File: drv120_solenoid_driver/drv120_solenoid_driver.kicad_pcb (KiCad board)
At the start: 2 copper layers, 23.6 x 13 mm, 9 parts, among them J1 +PWR-, J2 +EN-, J3 SOLENOID, U1 drv120

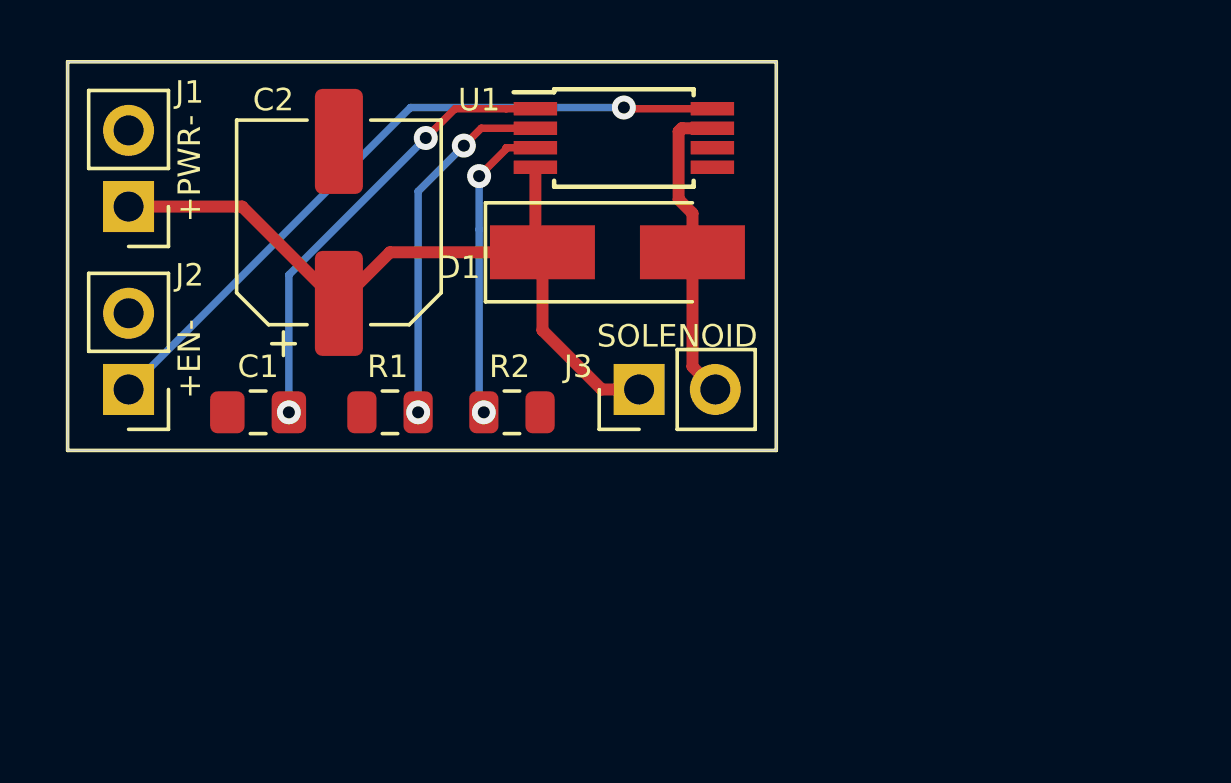
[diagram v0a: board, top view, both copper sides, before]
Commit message: Tab mounting version
PCB design with mounting tabs on either side
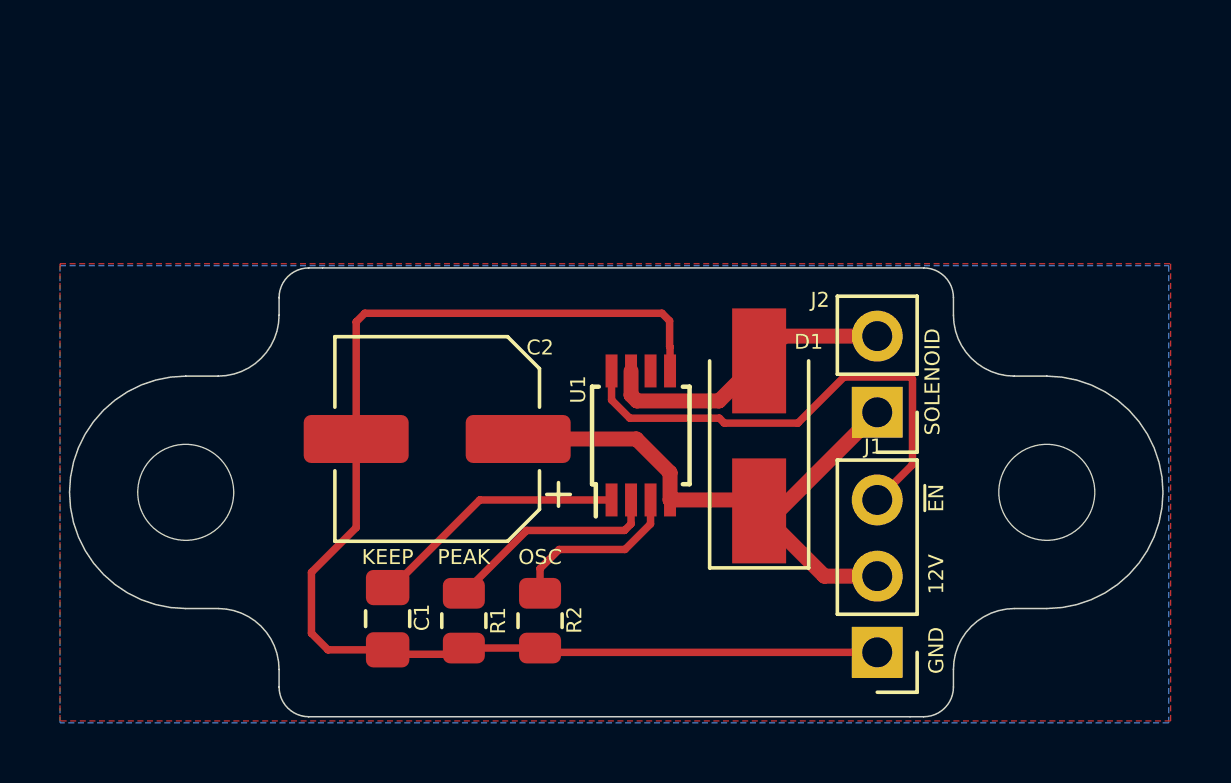
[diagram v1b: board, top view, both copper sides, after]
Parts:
- removed J3: SOLENOID, Connector_PinHeader_2.54mm:PinHeader_1x02_P2.54mm_Vertical
- added REF**: MountingHole_3.2mm_M3, MountingHole:MountingHole_3.2mm_M3, B.Cu at (166.8, 111.1)
- added REF**: MountingHole_3.2mm_M3, MountingHole:MountingHole_3.2mm_M3, B.Cu at (138.0, 111.1)
- C1: value 1u -> 4.7u; footprint Capacitor_SMD:C_0805_2012Metric_Pad1.15x1.40mm_HandSolder -> Capacitor_SMD:C_0805_2012Metric_Pad1.18x1.45mm_HandSolder
- J1: value +PWR- -> Control; footprint Connector_PinHeader_2.54mm:PinHeader_1x02_P2.54mm_Vertical -> Connector_PinHeader_2.54mm:PinHeader_1x03_P2.54mm_Vertical
- J2: value +EN- -> Solenoid
- R1: value 0 -> 47k
- U1: footprint Package_SO:TSSOP-8_4.4x3mm_P0.65mm -> Package_SO:TSSOP-8_3x3mm_P0.65mm
- moved J1 29.0 mm to (161.1, 116.5)
- moved J2 25.0 mm to (161.1, 108.5)
- moved U1 9.93 mm to (153.2, 109.2), turned to 90 degrees
- moved C1 8.12 mm to (144.8, 115.3), turned to 270 degrees
- moved C2 7.93 mm to (146.4, 109.3), turned to 180 degrees
- moved D1 7.73 mm to (157.2, 109.2), turned to 90 degrees
- moved R1 7.37 mm to (147.3, 115.4), turned to 270 degrees
- moved R2 7.01 mm to (149.9, 115.4), turned to 270 degrees
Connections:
- J1 pad 1: Net-(C2-Pad1) -> GND
- J1 pad 2: GND -> Net-(C2-Pad1)
- J2 pad 1: /Enable -> Net-(C2-Pad1)
- J2 pad 2: GND -> Net-(D1-Pad2)
- U1 pad 6: (no net) -> Net-(U1-Pad6)
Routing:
- net GND: track 0.00 -> 42.6 mm
- net /Enable: track 23.4 -> 16.5 mm, vias 1 -> 0
- net Net-(C1-Pad1): track 15.1 -> 8.73 mm, vias 2 -> 0
- net Net-(C2-Pad1): track 25.4 -> 19.7 mm
- net Net-(R1-Pad1): track 12.1 -> 7.33 mm, vias 2 -> 0
- net Net-(R2-Pad1): track 10.2 -> 5.92 mm, vias 2 -> 0
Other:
- board size 23.6 x 13 mm -> 36.4 x 15 mm
- rule pad_to_mask_clearance: 0.051 -> 0
- board text added: "12V"
- board text added: "GND"
- board text added: "KEEP"
- board text added: "OSC"
- board text added: "PEAK"
- board text added: "Rev: B"
- board text added: "SOLENOID"
- board text added: "https://github.com/MarkJB/ drv120_solenoid_driver_module"
- board text added: "~EN"

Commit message: Changed to JST-PH 2.00 TH connectors
Also changed input connector to a single 3 pin JST. Solenoid is on a 2 pin JST.
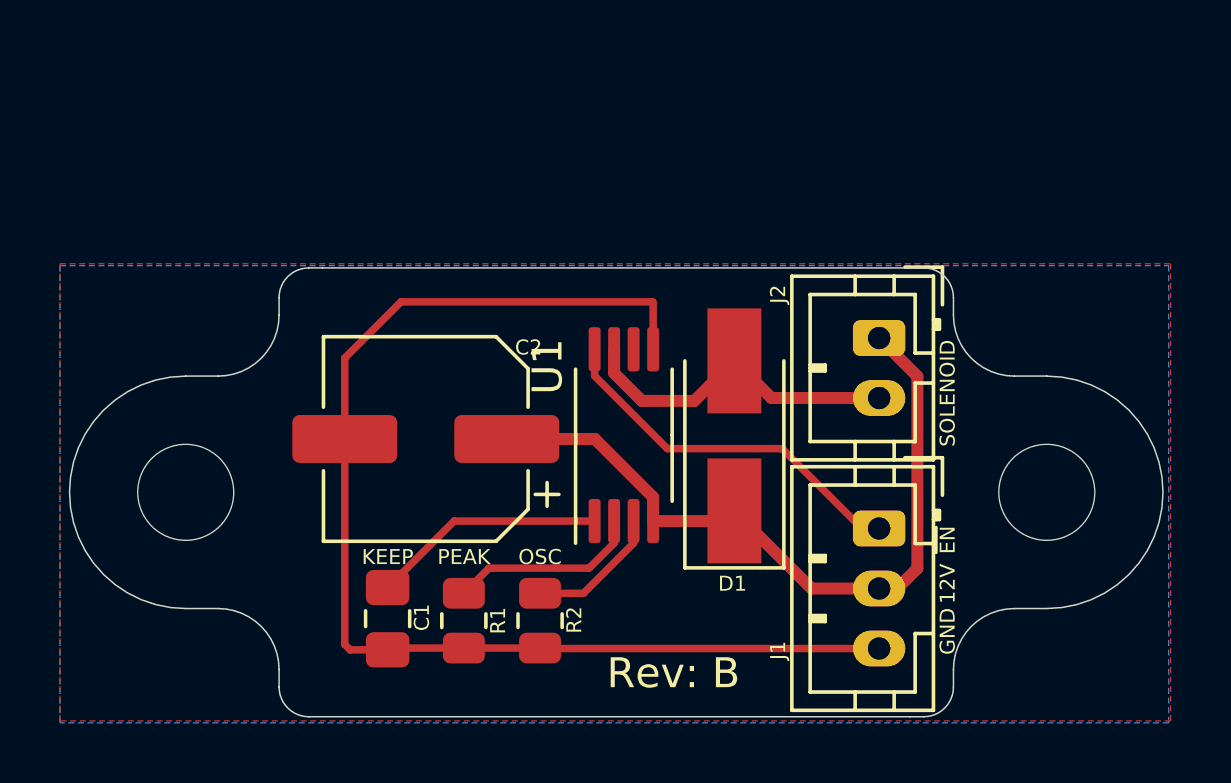
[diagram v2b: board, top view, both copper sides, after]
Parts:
- C1: value 4.7u -> 1u
- J1: value Control -> PWR/EN; footprint Connector_PinHeader_2.54mm:PinHeader_1x03_P2.54mm_Vertical -> Connector_JST:JST_PH_B3B-PH-K_1x03_P2.00mm_Vertical
- J2: footprint Connector_PinHeader_2.54mm:PinHeader_1x02_P2.54mm_Vertical -> Connector_JST:JST_PH_B2B-PH-K_1x02_P2.00mm_Vertical
- R1: value 47k -> 0
- U1: footprint Package_SO:TSSOP-8_3x3mm_P0.65mm -> Package_SO:TSSOP-8_4.4x3mm_P0.65mm
- moved J1 4.13 mm to (161.2, 112.3), turned to 270 degrees
- moved J2 2.48 mm to (161.2, 106.0), turned to 270 degrees
- moved D1 0.83 mm to (156.3, 109.2)
- moved U1 0.56 mm to (152.7, 109.2)
- moved C2 0.38 mm to (146.1, 109.3)
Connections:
- J1 pad 1: GND -> /Enable
- J1 pad 3: /Enable -> GND
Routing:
- net Net-(C2-Pad1): track 19.7 -> 25.0 mm
- net /Enable: track 16.5 -> 12.5 mm
- net GND: track 42.6 -> 40.3 mm
- net Net-(D1-Pad2): track 9.99 -> 12.1 mm
- net Net-(R2-Pad1): track 5.92 -> 4.55 mm
- net Net-(C1-Pad1): track 8.73 -> 7.82 mm
- net Net-(R1-Pad1): track 7.33 -> 6.44 mm
